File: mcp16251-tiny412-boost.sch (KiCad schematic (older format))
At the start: 33 parts, among them J1 THT_Castellated, J2 JST_PH_Header, J3 THT_Castellated, J4 THT_Castellated, J5 THT_Castellated, J6 THT_Castellated, Q1 Q_PMOS_GSD, Q2 NPN_3904, Q3 Q_PMOS_GSD, Q4 Q_PMOS_GSD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

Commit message: Major components
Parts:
- added C? (x3): 0.1uF, symbol Device:C_Small
- added R?: 3.3k, symbol Device:R
- added R? (x2): R, symbol Device:R_Small
- added U?: attiny412, symbol local_symbols:attiny412
- added U?: AP7354, symbol local_symbols:AP7354
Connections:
- net labels added: 2V5, PA1, PA2, PA3, UPDI
- wire segments 90 -> 123
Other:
- note added: "3.0V-4.2V"
- note added: "Battery input and protection"
- note added: "MCP16251T (SOT-23-6)\nvoltage boost regulator\n(pin compatible: TPS6107x)"
- note removed: "MCP16251T (SOT-23-6)\nvoltage boost regulator"
- note removed: "Raw VBAT input, power-off circuit,\nvoltage supervisor for boost converter"
- moved on the sheet: C3, F1, J1, J2, J3, J4, J5, J6, JP1, JP2, Q1, Q2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

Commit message: Further schematic work
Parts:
- added J? (x7): THT_Castellated, MCP16251_module:Conn_01x01_cast, symbol Connector_Generic:Conn_01x01
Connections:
- net labels added: PA1_HV, PA2_HV, UPDI_HV
- wire segments 123 -> 126
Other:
- note added: "2.5V for AVR controller"
- note added: "Attiny412 MCU"
- note added: "External connectors, headers, etc"
- note added: "max 2.5V"
- moved on the sheet: C?, F1, J1, J2, J3, J4, J5, J6, JP1, Q1, R?, SW1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

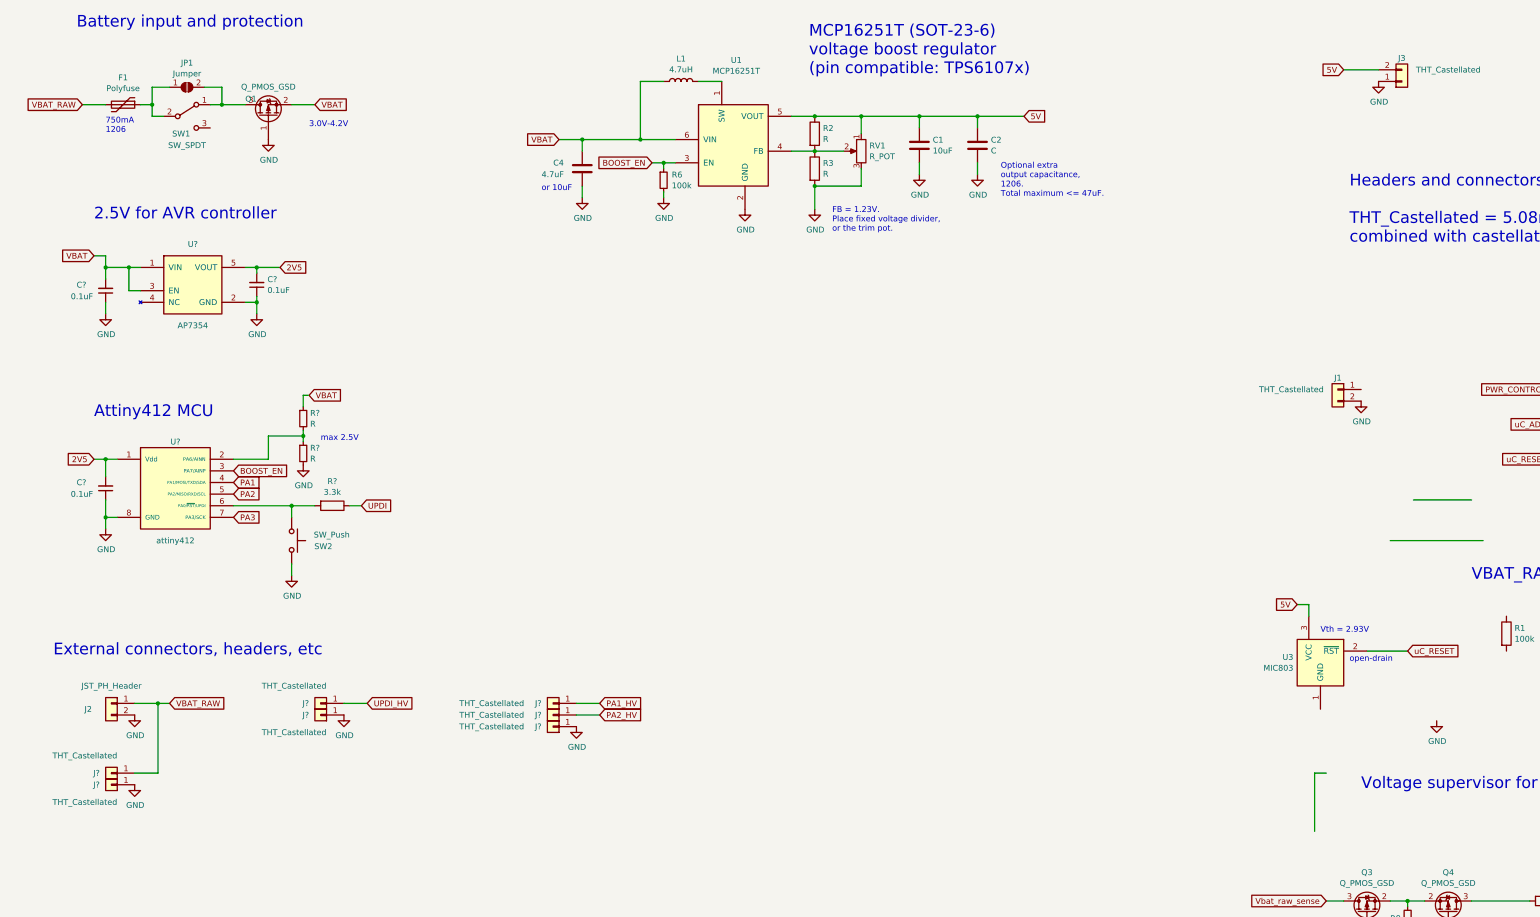
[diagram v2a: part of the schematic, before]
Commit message: Add logic level shifter TXB104
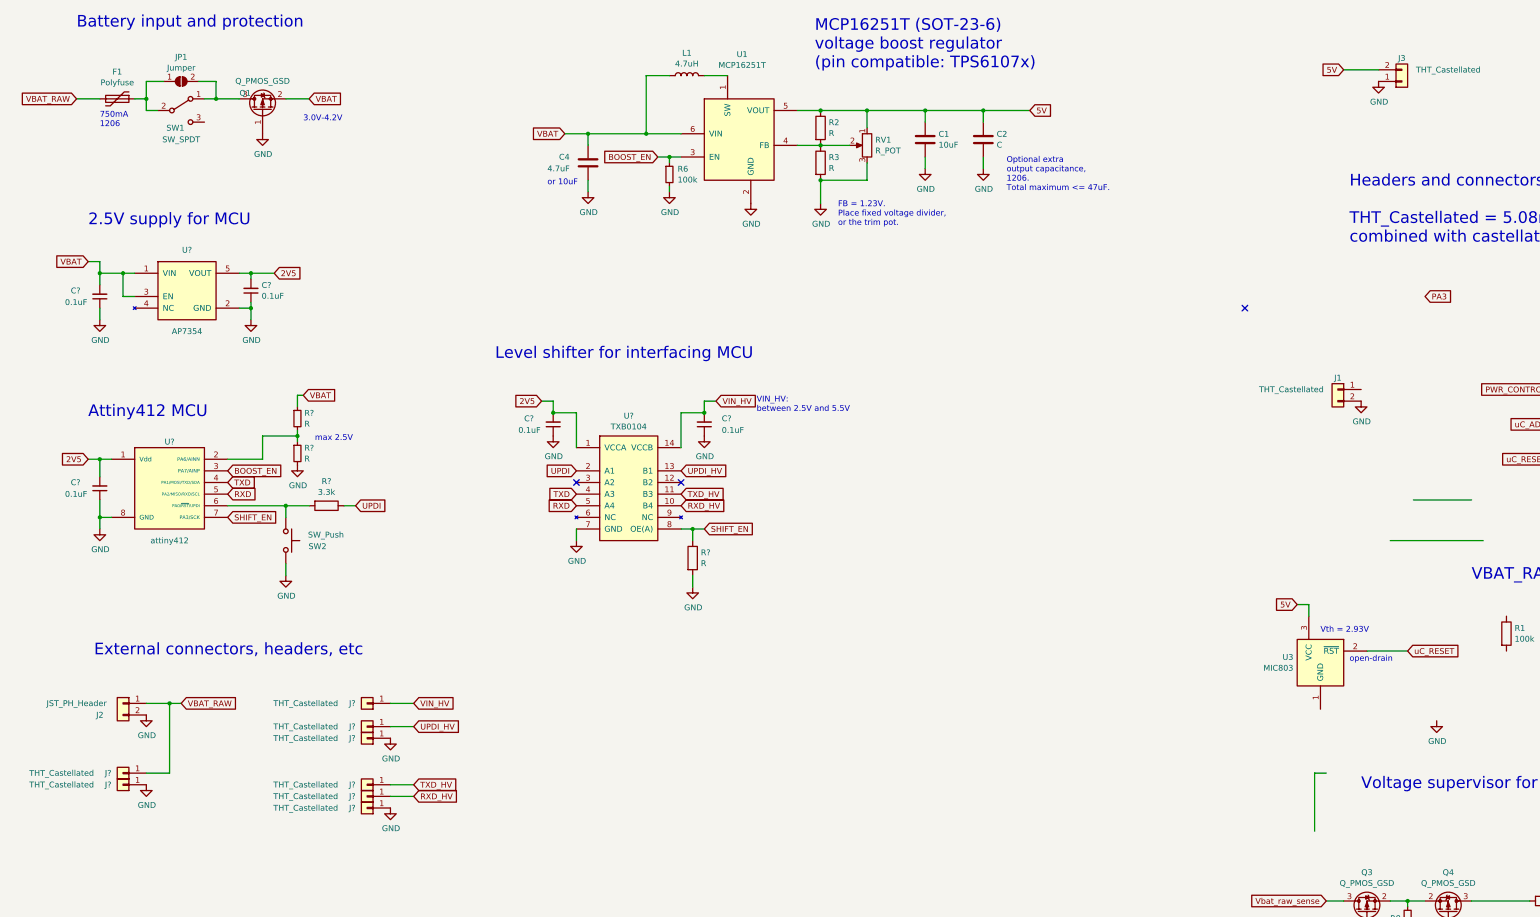
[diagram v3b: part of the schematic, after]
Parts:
- added C? (x2): 0.1uF, symbol Device:C_Small
- added J?: THT_Castellated, MCP16251_module:Conn_01x01_cast, symbol Connector_Generic:Conn_01x01
- added R?: R, MCP16251_module:R_0805_HS, symbol Device:R
- added U?: TXB0104, symbol local_symbols:TXB0104
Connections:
- net labels added: RXD, RXD_HV, SHIFT_EN, TXD, TXD_HV, VIN_HV
- net labels removed: PA1, PA1_HV, PA2, PA2_HV
- wire segments 126 -> 140
- no-connect marks 1 -> 4
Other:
- note added: "2.5V supply for MCU"
- note added: "Level shifter for interfacing MCU"
- note added: "VIN_HV:\nbetween 2.5V and 5.5V"
- note removed: "2.5V for AVR controller"
- moved on the sheet: C1, C2, C4, C?, F1, J2, J?, JP1, L1, Q1, R2, R3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

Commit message: Initial complete design, needs proof-reading
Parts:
- removed C3: 100nF, MCP16251_module:R_0805_HS, symbol Device:C
- removed J1: THT_Castellated, MCP16251_module:Conn_01x02_cast, symbol Connector_Generic:Conn_01x02
- removed J3: THT_Castellated, MCP16251_module:Conn_01x02_cast_mirrored, symbol Connector_Generic:Conn_01x02
- removed J4, J5, J6: THT_Castellated, MCP16251_module:Conn_01x01_cast, symbol Connector_Generic:Conn_01x01
- removed JP2: Jumper, MCP16251_module:R_0805_HS, symbol Jumper:SolderJumper_2_Open
- removed Q2: NPN_3904, MCP16251_module:SOT-23_HS, symbol Device:Q_NPN_BEC
- removed Q3, Q4: Q_PMOS_GSD, MCP16251_module:SOT-23_HS, symbol Device:Q_PMOS_GSD
- removed R1: 100k, MCP16251_module:R_0805_HS, symbol Device:R
- removed R4, R5, R8: 100k, MCP16251_module:R_0805_HS, symbol Device:R_Small
- removed R7: 1k, MCP16251_module:R_0805_HS, symbol Device:R
- removed U3: MIC803, MCP16251_module:SOT-23_HS, symbol local_symbols:MIC803
- removed U4: MIC2777, MCP16251_module:SOT-23-5_HS, symbol local_symbols:MIC2777
- added J? (x2): THT_Castellated, MCP16251_module:Conn_01x01_cast, symbol Connector_Generic:Conn_01x01
- added JP?: Jumper, MCP16251_module:R_0805_HS, symbol Jumper:SolderJumper_2_Open
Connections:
- net labels removed: PA3, PWR_CONTROL, Vbat_raw_sense, uC_ADC, uC_RESET
- wire segments 140 -> 101
- no-connect marks 4 -> 1
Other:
- note added: "Boost output to VIN_HV"
- note added: "Supervisor for level shifter"
- note removed: "Headers and connectors;\n\nTHT_Castellated = 5.08mm screw terminal,\ncombined with castellated edge"
- note removed: "VBAT_RAW voltage switch"
- note removed: "Voltage supervisor for microcontroller"
- note removed: "Vth = 4.68V"
- note removed: "open-drain"
- moved on the sheet: C?, R?, U2, U?

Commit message: Annotate schematic, prepare footprints
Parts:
- added C8: 0.1uF, MCP16251_module:0805_HS, symbol Device:C_Small
- C1, C2, C4, F1: footprint MCP16251_module:R_1206_HS -> MCP16251_module:1206_HS
- C10, C11, C5, C6, C7: renamed from C?; footprint (none) -> MCP16251_module:0805_HS
- JP1, R2, R3: footprint MCP16251_module:R_0805_HS -> MCP16251_module:0805_HS
- JP2: renamed from JP?; footprint MCP16251_module:R_0805_HS -> MCP16251_module:0805_HS
- R5: renamed from R6; footprint MCP16251_module:R_0805_HS -> MCP16251_module:0805_HS
- R6, R7, R8: renamed from R?; footprint (none) -> MCP16251_module:0805_HS
- R9: renamed from R?; value R -> 100k; footprint MCP16251_module:R_0805_HS -> MCP16251_module:0805_HS
- SW2: footprint Buttons_Switches_SMD:SW_SPST_TL3342 -> MCP16251_module:SW_SPST_PUSH_6mm_3mm
- U3: renamed from U?; footprint (none) -> MCP16251_module:SOIC-8_3.9x4.9mm_Pitch1.27_HSmm
- U4: renamed from U?; footprint (none) -> MCP16251_module:SOT-23-5_HS
- U5: renamed from U?; footprint (none) -> MCP16251_module:SOIC-14_3.9x8.7mm_Pitch1.27mm_HS
- gave numbers to parts that had none: 10
- renumbered J2 to J1
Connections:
- net GND: now also C8.1
- net at R6.2, R7.1, U3.2 (PA6/AINN): now also C8.2
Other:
- moved on the sheet: R6, R7, SW2
